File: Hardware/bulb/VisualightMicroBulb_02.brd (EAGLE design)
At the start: 47.4 x 34 mm, 27 parts, among them SW1 SPST_TACT-KMR2, U1 MIC5219 3.3V, U3 ATMEGA32U4, X2 USBPCB, Y1 16MHz

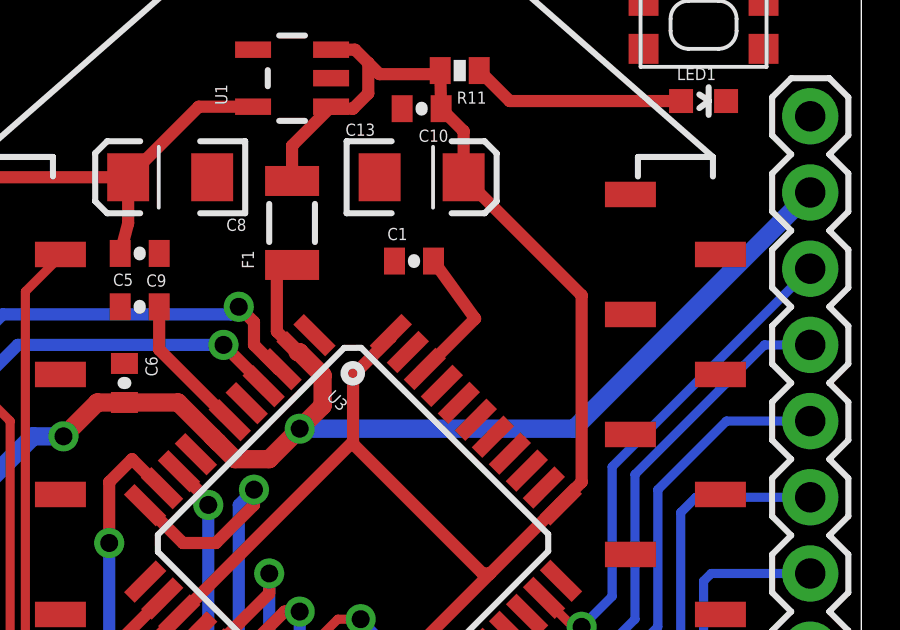
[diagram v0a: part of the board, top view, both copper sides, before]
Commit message: Updates to firmware with MAC address and hardware with ground planes
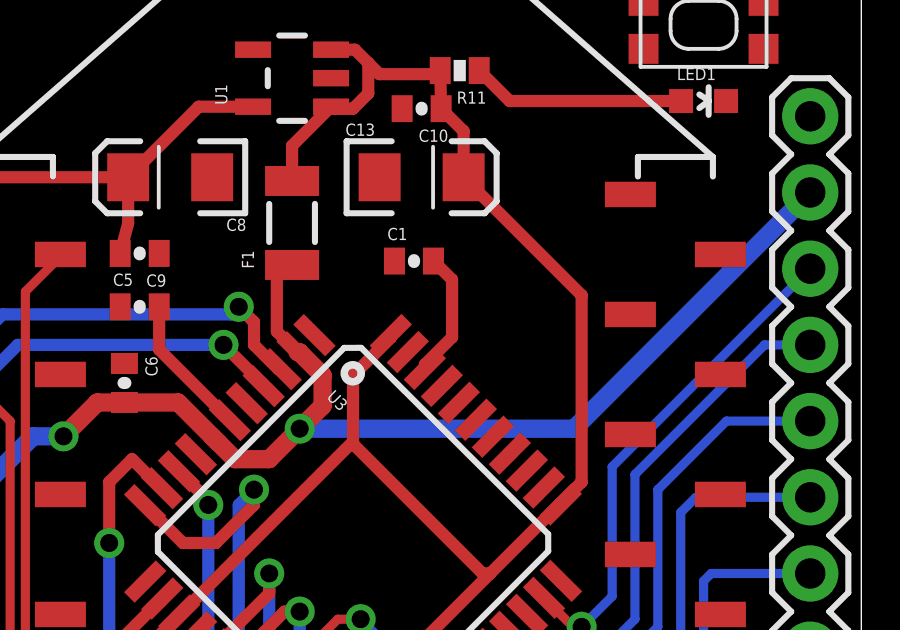
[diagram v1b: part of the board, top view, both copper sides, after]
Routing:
- net AREF: track 4.74 -> 4.23 mm
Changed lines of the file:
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@@
 <contactref element="C1" pad="2"/>
 <contactref element="U3" pad="42"/>
-<wire x1="58.7820375" y1="53.0464625" x2="60.457575" y2="54.722" width="0.4064" layer="1"/>
-<wire x1="60.457575" y1="54.722" x2="59.07" y2="56.642" width="0.4064" layer="1"/>
+<wire x1="59.07" y1="56.642" x2="59.69" y2="56.022" width="0.4064" layer="1"/>
+<wire x1="59.69" y1="56.022" x2="59.69" y2="54.102" width="0.4064" layer="1"/>
+<wire x1="59.69" y1="54.102" x2="58.7820375" y2="53.1940375" width="0.4064" layer="1"/>
+<wire x1="58.7820375" y1="53.1940375" x2="58.7820375" y2="53.0464625" width="0.4064" layer="1"/>
 </signal>
 <signal name="RESET">
